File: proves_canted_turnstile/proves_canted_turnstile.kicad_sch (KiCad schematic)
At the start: 26 parts, among them J1 Conn_Coaxial, J2 Conn_02x02_Counter_Clockwise, U1 QBA-07+, U2 QBA-07+, U3 QBA-07+

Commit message: porting proves features
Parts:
- removed J2: Conn_02x02_Counter_Clockwise, Connector_Hirose:Hirose_DF11-4DP-2DSA_2x02_P2.00mm_Vertical, symbol Connector_Generic:Conn_02x02_Counter_Clockwise
- added J10: WDT Disable Jumper, Connector_PinHeader_2.54mm:PinHeader_1x02_P2.54mm_Vertical, symbol Connector_Generic:Conn_01x02
- added J11: DEBUG, Connector_Hirose:Hirose_DF11-12DP-2DSA_2x06_P2.00mm_Vertical, symbol Connector_Generic:Conn_02x06_Odd_Even
- added J12, J8: USB_C_Receptacle_USB2.0_16P, Connector_USB:USB_C_Receptacle_HRO_TYPE-C-31-M-12, symbol Connector:USB_C_Receptacle_USB2.0_16P
- added J3: Battery Charge Bypass, Connector_PinHeader_2.54mm:PinHeader_1x02_P2.54mm_Vertical, symbol Connector_Generic:Conn_01x02
- added J6: FC Reset Jumper, Connector_PinHeader_2.54mm:PinHeader_1x02_P2.54mm_Vertical, symbol Connector_Generic:Conn_01x02
- added J7: FC USB Bootselect Jumper, Connector_PinHeader_2.54mm:PinHeader_1x02_P2.54mm_Vertical, symbol Connector_Generic:Conn_01x02
- added J9: DF11-4DP-2DSA, Connector_Hirose:Hirose_DF11-4DP-2DSA_2x02_P2.00mm_Vertical, symbol Connector_Generic:Conn_02x02_Odd_Even
- added R26, R27, R5, R6: 5.1k, Resistor_SMD:R_0603_1608Metric, symbol mainboard:RESISTOR0603
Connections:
- net GND: now also J10.2 (Pin_2), J11.1 (Pin_1), J11.2 (Pin_2), J12.A1 (GND), J12.A12 (GND), J12.B1 (GND), J12.B12 (GND), J12.S1 (SHIELD), J3.2 (Pin_2), J6.2 (Pin_2), J7.2 (Pin_2), J8.A1 (GND), J8.A12 (GND), J8.B1 (GND), J8.B12 (GND), J8.S1 (SHIELD), J9.4 (Pin_4), R26.1, R27.1, R5.1, R6.1
- net BURN: now reaches R4.1
- net BURN: now also J11.4 (Pin_4)
- new net: J8.A5 (CC1), R5.2
- new net: J8.B5 (CC2), R6.2
- new net: J12.A4 (VBUS), J12.A9 (VBUS), J12.B4 (VBUS), J12.B9 (VBUS)
- new net: J12.A5 (CC1), R26.2
- new net: J12.B5 (CC2), R27.2
- new net +3V3: J11.8 (Pin_8)
- new net Dir_Chrg_In: J11.6 (Pin_6), J3.1 (Pin_1)
- new net FC_USBBOOT: J11.11 (Pin_11), J7.1 (Pin_1)
- new net Payload_D+: J8.A6 (D+), J8.B6 (D+), J9.3 (Pin_3)
- new net Payload_D-: J8.A7 (D-), J8.B7 (D-), J9.1 (Pin_1)
- new net Payload_VBUS: J8.A4 (VBUS), J8.A9 (VBUS), J8.B4 (VBUS), J8.B9 (VBUS), J9.2 (Pin_2)
- new net USB_D+: J11.9 (Pin_9), J12.A6 (D+), J12.B6 (D+)
- new net USB_D-: J11.10 (Pin_10), J12.A7 (D-), J12.B7 (D-)
- new net WDT_DISABLE: J10.1 (Pin_1), J11.3 (Pin_3)
- new net ~{FC_RESET}: J11.12 (Pin_12), J6.1 (Pin_1)
- no-connect marks 0 -> 7
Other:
- note added: "Debug Passthroughs"
- note added: "FC Board Connection"
- note added: "Payload Board Connection"
- moved on the sheet: AE1, AE2, AE3, AE4, H1, H2, H3, H4, H5, H6, H7, J1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

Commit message: Finished board
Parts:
- removed H5, H6, H7: MountingHole, MountingHole:MountingHole_2.7mm_M2.5_Pad, symbol Mechanical:MountingHole
- R4: footprint Resistor_THT:R_Axial_DIN0411_L9.9mm_D3.6mm_P25.40mm_Horizontal -> Resistor_THT:R_Axial_DIN0309_L9.0mm_D3.2mm_P12.70mm_Horizontal
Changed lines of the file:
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@@
 	)
 	(symbol
-		(lib_id "Mechanical:MountingHole")
-		(at 365.76 58.42 0)
-		(unit 1)
-		(exclude_from_sim yes)
-		(in_bom no)
-		(on_board yes)
-		(dnp no)
-		(fields_autoplaced yes)
-		(property "Reference" "H6"
-			(at 368.3 57.1499 0)
-			(effects
-				(font
-					(size 1.27 1.27)
-				)
-				(justify left)
-			)
-		)
-		(property "Value" "MountingHole"
-			(at 368.3 59.6899 0)
-			(effects
-				(font
-					(size 1.27 1.27)
-				)
-				(justify left)
-			)
-		)
-		(property "Footprint" "MountingHole:MountingHole_2.7mm_M2.5_Pad"
-			(at 365.76 58.42 0)
-			(effects
-				(font
-					(size 1.27 1.27)
-				)
-				(hide yes)
-			)
-		)
-		(property "Datasheet" "~"
-			(at 365.76 58.42 0)
-			(effects
-				(font
-					(size 1.27 1.27)
-				)
-				(hide yes)
-			)
-		)
-		(property "Description" "Mounting Hole without connection"
-			(at 365.76 58.42 0)
-			(effects
-				(font
-					(size 1.27 1.27)
-				)
-				(hide yes)
-			)
-		)
-		(instances
-			(project "proves_canted_turnstile"
-				(path "/b0a1b345-df47-405c-b751-07790b55dab3"
-					(reference "H6")
-					(unit 1)
-				)
-			)
-		)
-	)
-	(symbol
 		(lib_id "plusz-end-card-with-turnstile-mezzanine-eagle-import:QBA-07+")
 		(at 100.33 73.66 0)
@@
 			)
 		)
-		(property "Footprint" "Resistor_THT:R_Axial_DIN0411_L9.9mm_D3.6mm_P25.40mm_Horizontal"
+		(property "Footprint" "Resistor_THT:R_Axial_DIN0309_L9.0mm_D3.2mm_P12.70mm_Horizontal"
 			(at 356.87 185.42 0)
 			(effects
@@
 	)
 	(symbol
-		(lib_id "Mechanical:MountingHole")
-		(at 331.47 58.42 0)
-		(unit 1)
-		(exclude_from_sim yes)
-		(in_bom no)
-		(on_board yes)
-		(dnp no)
-		(fields_autoplaced yes)
-		(property "Reference" "H5"
-			(at 334.01 57.1499 0)
-			(effects
-				(font
-					(size 1.27 1.27)
-				)
-				(justify left)
-			)
-		)
-		(property "Value" "MountingHole"
-			(at 334.01 59.6899 0)
-			(effects
-				(font
-					(size 1.27 1.27)
-				)
-				(justify left)
-			)
-		)
-		(property "Footprint" "MountingHole:MountingHole_2.7mm_M2.5_Pad"
-			(at 331.47 58.42 0)
-			(effects
-				(font
-					(size 1.27 1.27)
-				)
-				(hide yes)
-			)
-		)
-		(property "Datasheet" "~"
-			(at 331.47 58.42 0)
-			(effects
-				(font
-					(size 1.27 1.27)
-				)
-				(hide yes)
-			)
-		)
-		(property "Description" "Mounting Hole without connection"
-			(at 331.47 58.42 0)
-			(effects
-				(font
-					(size 1.27 1.27)
-				)
-				(hide yes)
-			)
-		)
-		(instances
-			(project "proves_canted_turnstile"
-				(path "/b0a1b345-df47-405c-b751-07790b55dab3"
-					(reference "H5")
-					(unit 1)
-				)
-			)
-		)
-	)
-	(symbol
 		(lib_id "Connector_Generic:Conn_01x02")
 		(at 320.04 220.98 0)
@@
 					(unit 1)
 				)
-			)
-		)
-	)
-	(symbol
-		(lib_id "Mechanical:MountingHole")
-		(at 393.7 58.42 0)
-		(unit 1)
-		(exclude_from_sim yes)
-		(in_bom no)
-		(on_board yes)
-		(dnp no)
-		(fields_autoplaced yes)
-		(property "Reference" "H7"
-			(at 396.24 57.1499 0)
-			(effects
-				(font
-					(size 1.27 1.27)
-				)
-				(justify left)
-			)
-		)
-		(property "Value" "MountingHole"
-			(at 396.24 59.6899 0)
-			(effects
-				(font
-					(size 1.27 1.27)
-				)
-				(justify left)
-			)
-		)
-		(property "Footprint" "MountingHole:MountingHole_2.7mm_M2.5_Pad"
-			(at 393.7 58.42 0)
-			(effects
-				(font
-					(size 1.27 1.27)
-				)
-				(hide yes)
-			)
-		)
-		(property "Datasheet" "~"
-			(at 393.7 58.42 0)
-			(effects
-				(font
-					(size 1.27 1.27)
-				)
-				(hide yes)
-			)
-		)
-		(property "Description" "Mounting Hole without connection"
-			(at 393.7 58.42 0)
-			(effects
-				(font
-					(size 1.27 1.27)
-				)
-				(hide yes)
-			)
-		)
-		(instances
-			(project "proves_canted_turnstile"
-				(path "/b0a1b345-df47-405c-b751-07790b55dab3"
-					(reference "H7")
-					(unit 1)
-				)

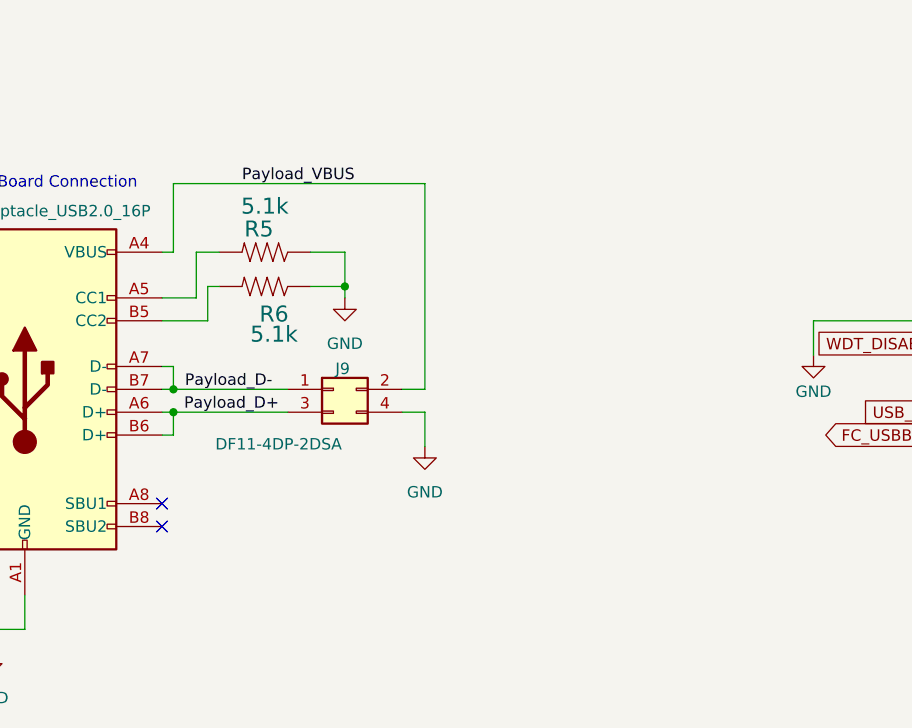
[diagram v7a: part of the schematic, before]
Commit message: adjusted antenna landing pads
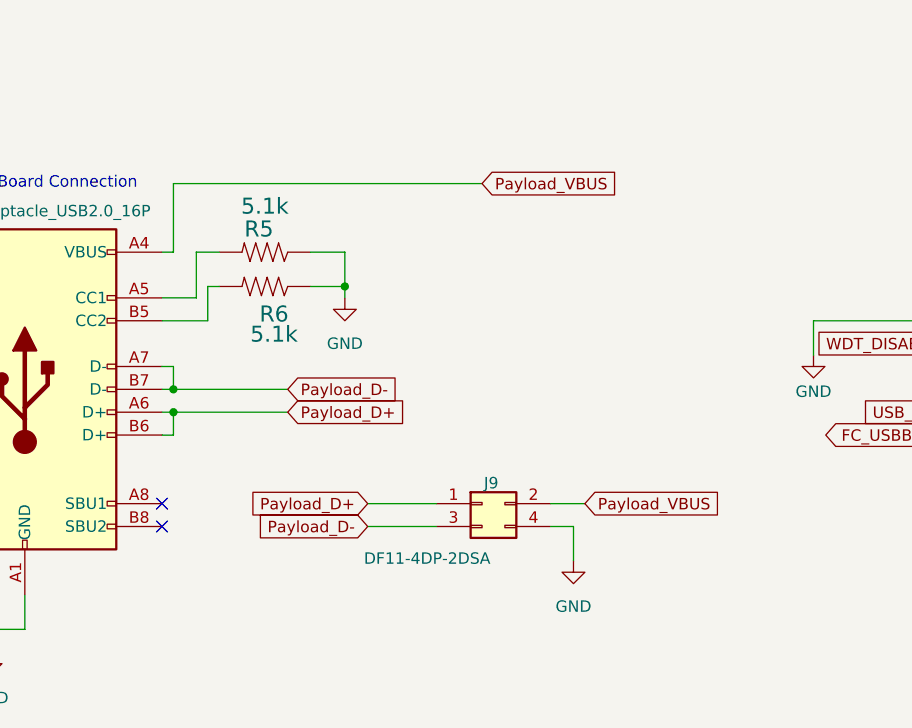
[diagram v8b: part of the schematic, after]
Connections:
- net Payload_D+: now also J9.1 (Pin_1); no longer J9.3 (Pin_3)
- net Payload_D-: now also J9.3 (Pin_3); no longer J9.1 (Pin_1)
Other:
- moved on the sheet: J9
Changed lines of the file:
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@@
 	)
 	(junction
-		(at 137.16 227.33)
+		(at 68.58 223.52)
 		(diameter 0)
 		(color 0 0 0 0)
 	)
 	(junction
-		(at 68.58 223.52)
+		(at 45.72 247.65)
 		(diameter 0)
 		(color 0 0 0 0)
 	)
 	(junction
-		(at 137.16 224.79)
+		(at 68.58 220.98)
 		(diameter 0)
 		(color 0 0 0 0)
 	)
 	(junction
-		(at 45.72 247.65)
+		(at 116.84 251.46)
 		(diameter 0)
 		(color 0 0 0 0)
 	)
 	(junction
-		(at 68.58 220.98)
+		(at 137.16 224.79)
 		(diameter 0)
 		(color 0 0 0 0)
 	)
 	(junction
-		(at 116.84 251.46)
+		(at 156.21 213.36)
 		(diameter 0)
 		(color 0 0 0 0)
 	)
 	(junction
-		(at 156.21 213.36)
+		(at 137.16 227.33)
 		(diameter 0)
 		(color 0 0 0 0)
@@
 	(wire
 		(pts
-			(xy 165.1 201.93) (xy 165.1 224.79)
-		)
-		(stroke
-			(width 0)
-			(type default)
-		)
-	)
-	(wire
-		(pts
 			(xy 120.65 247.65) (xy 120.65 251.46)
 		)
@@
 	(wire
 		(pts
-			(xy 327.66 223.52) (xy 327.66 224.79)
+			(xy 158.75 240.03) (xy 166.37 240.03)
 		)
 		(stroke
@@
 	(wire
 		(pts
-			(xy 123.19 53.34) (xy 166.37 53.34)
-		)
-		(stroke
-			(width 0.1524)
-			(type solid)
-		)
-	)
-	(wire
-		(pts
-			(xy 137.16 224.79) (xy 135.89 224.79)
+			(xy 327.66 223.52) (xy 327.66 224.79)
 		)
 		(stroke
@@
 	(wire
 		(pts
-			(xy 325.12 223.52) (xy 327.66 223.52)
+			(xy 123.19 53.34) (xy 166.37 53.34)
 		)
 		(stroke
-			(width 0)
-			(type default)
+			(width 0.1524)
+			(type solid)
 		)
 	)
 	(wire
 		(pts
-			(xy 165.1 224.79) (xy 162.56 224.79)
+			(xy 325.12 223.52) (xy 327.66 223.52)
 		)
 		(stroke
@@
 	(wire
 		(pts
-			(xy 137.16 201.93) (xy 165.1 201.93)
+			(xy 137.16 201.93) (xy 171.45 201.93)
 		)
 		(stroke
@@
 	(wire
 		(pts
-			(xy 165.1 227.33) (xy 165.1 231.14)
+			(xy 181.61 240.03) (xy 181.61 243.84)
 		)
 		(stroke
@@
 		)
 	)
-	(wire
-		(pts
-			(xy 137.16 224.79) (xy 149.86 224.79)
-		)
-		(stroke
-			(width 0)
-			(type default)
-		)
-	)
 	(polyline
 		(pts
@@
 	(wire
 		(pts
+			(xy 137.16 224.79) (xy 149.86 224.79)
+		)
+		(stroke
+			(width 0)
+			(type default)
+		)
+	)
+	(wire
+		(pts
 			(xy 100.33 83.82) (xy 100.33 93.98)
 		)
@@
 	(wire
 		(pts
+			(xy 179.07 237.49) (xy 182.88 237.49)
+		)
+		(stroke
+			(width 0)
+			(type default)
+		)
+	)
+	(wire
+		(pts
 			(xy 81.28 209.55) (xy 85.09 209.55)
 		)
@@
 	(wire
 		(pts
+			(xy 135.89 224.79) (xy 137.16 224.79)
+		)
+		(stroke
+			(width 0)
+			(type default)
+		)
+	)
+	(wire
+		(pts
 			(xy 222.25 60.96) (xy 222.25 66.04)
 		)
@@
 	(wire
 		(pts
-			(xy 162.56 227.33) (xy 165.1 227.33)
+			(xy 179.07 240.03) (xy 181.61 240.03)
 		)
 		(stroke
@@
 		)
 	)
-	(label "Payload_D-"
-		(at 138.43 224.79 0)
-		(effects
-			(font
-				(size 1.27 1.27)
-			)
-			(justify left bottom)
+	(wire
+		(pts
+			(xy 158.75 237.49) (xy 166.37 237.49)
+		)
+		(stroke
+			(width 0)
+			(type default)
 		)
 	)
@@
 		)
 	)
-	(label "Payload_D+"
-		(at 138.3421 227.33 0)
-		(effects
-			(font
-				(size 1.27 1.27)
-			)
-			(justify left bottom)
-		)
-	)
 	(label "UHF_180"
 		(at 204.47 104.14 0)
@@
 		)
 	)
-	(label "Payload_VBUS"
-		(at 144.78 201.93 0)
-		(effects
-			(font
-				(size 1.27 1.27)
-			)
-			(justify left bottom)
-		)
-	)
 	(label "UHF_0"
 		(at 204.47 53.34 0)
@@
 		)
 	)
+	(global_label "Payload_D-"
+		(shape input)
+		(at 158.75 240.03 180)
+		(fields_autoplaced yes)
+		(effects
+			(font
+				(size 1.27 1.27)
+			)
+			(justify right)
+		)
+		(property "Intersheetrefs" "${INTERSHEET_REFS}"
+			(at 144.456 240.03 0)
+			(effects
+				(font
+					(size 1.27 1.27)
+				)
+				(justify right)
+				(hide yes)
+			)
+		)
+	)
+	(global_label "Payload_VBUS"
+		(shape input)
+		(at 182.88 237.49 0)
+		(fields_autoplaced yes)
+		(effects
+			(font
+				(size 1.27 1.27)
+			)
+			(justify left)
+		)
+		(property "Intersheetrefs" "${INTERSHEET_REFS}"
+			(at 199.2302 237.49 0)
+			(effects
+				(font
+					(size 1.27 1.27)
+				)
+				(justify left)
+				(hide yes)
+			)
+		)
+	)
+	(global_label "Payload_D+"
+		(shape input)
+		(at 149.86 227.33 0)
+		(fields_autoplaced yes)
+		(effects
+			(font
+				(size 1.27 1.27)
+			)
+			(justify left)
+		)
+		(property "Intersheetrefs" "${INTERSHEET_REFS}"
+			(at 164.154 227.33 0)
+			(effects
+				(font
+					(size 1.27 1.27)
+				)
+				(justify left)
+				(hide yes)
+			)
+		)
+	)
 	(global_label "~{FC_RESET}"
 		(shape output)
@@
 		)
 	)
+	(global_label "Payload_D-"
+		(shape input)
+		(at 149.86 224.79 0)
+		(fields_autoplaced yes)
+		(effects
+			(font
+				(size 1.27 1.27)
+			)
+			(justify left)
+		)
+		(property "Intersheetrefs" "${INTERSHEET_REFS}"
+			(at 164.154 224.79 0)
+			(effects
+				(font
+					(size 1.27 1.27)
+				)
+				(justify left)
+				(hide yes)
+			)
+		)
+	)
 	(global_label "WDT_DISABLE"
 		(shape input)
@@
 		)
 	)
+	(global_label "Payload_D+"
+		(shape input)
+		(at 158.75 237.49 180)
+		(fields_autoplaced yes)
+		(effects
+			(font
+				(size 1.27 1.27)
+			)
+			(justify right)
+		)
+		(property "Intersheetrefs" "${INTERSHEET_REFS}"
+			(at 144.456 237.49 0)
+			(effects
+				(font
+					(size 1.27 1.27)
+				)
+				(justify right)
+				(hide yes)
+			)
+		)
+	)
 	(global_label "WDT_DISABLE"
 		(shape input)
@@
 		)
 	)
+	(global_label "Payload_VBUS"
+		(shape input)
+		(at 171.45 201.93 0)
+		(fields_autoplaced yes)
+		(effects
+			(font
+				(size 1.27 1.27)
+			)
+			(justify left)
+		)
+		(property "Intersheetrefs" "${INTERSHEET_REFS}"
+			(at 187.8002 201.93 0)
+			(effects
+				(font
+					(size 1.27 1.27)
+				)
+				(justify left)
+				(hide yes)
+			)
+		)
+	)
 	(global_label "USB_D+"
 		(shape input)
@@
 		(lib_name "GND_1")
 		(lib_id "power:GND")
-		(at 165.1 231.14 0)
+		(at 181.61 243.84 0)
 		(unit 1)
 		(exclude_from_sim no)
@@
 		(fields_autoplaced yes)
 		(property "Reference" "#PWR05"
-			(at 165.1 237.49 0)
+			(at 181.61 250.19 0)
 			(effects
 				(font
@@
 		)
 		(property "Value" "GND"
-			(at 165.1 236.22 0)
+			(at 181.61 248.92 0)
 			(effects
 				(font
@@
 		)
 		(property "Footprint" ""
-			(at 165.1 231.14 0)
+			(at 181.61 243.84 0)
 			(effects
 				(font
@@
 		)
 		(property "Datasheet" ""
-			(at 165.1 231.14 0)
+			(at 181.61 243.84 0)
 			(effects
 				(font
@@
 		)
 		(property "Description" "Power symbol creates a global label with name \"GND\" , ground"
-			(at 165.1 231.14 0)
+			(at 181.61 243.84 0)
 			(effects
 				(font
@@
 	(symbol
 		(lib_id "Connector_Generic:Conn_02x02_Odd_Even")
-		(at 154.94 224.79 0)
+		(at 171.45 237.49 0)
 		(unit 1)
 		(exclude_from_sim no)
@@
 		(dnp no)
 		(property "Reference" "J9"
-			(at 155.956 222.504 0)
+			(at 172.466 235.204 0)
 			(effects
 				(font
@@
 		)
 		(property "Value" "DF11-4DP-2DSA"
-			(at 148.844 230.886 0)
+			(at 165.354 243.586 0)
 			(effects
 				(font
@@
 		)
 		(property "Footprint" "Connector_Hirose:Hirose_DF11-4DP-2DSA_2x02_P2.00mm_Vertical"
-			(at 154.94 224.79 0)
+			(at 171.45 237.49 0)
 			(effects
 				(font
@@
 		)
 		(property "Datasheet" "~"
-			(at 154.94 224.79 0)
+			(at 171.45 237.49 0)
 			(effects
 				(font
@@
 		)
 		(property "Description" "Generic connector, double row, 02x02, odd/even pin numbering scheme (row 1 odd numbers, row 2 even numbers), script generated (kicad-library-utils/schlib/autogen/connector/)"
-			(at 154.94 224.79 0)
+			(at 171.45 237.49 0)
 			(effects
 				(font
